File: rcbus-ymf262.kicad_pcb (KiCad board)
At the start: 2 copper layers, 100 x 50 mm, 43 parts, among them CON1 SJ1-3523N, P1 RC2014 BUS, U1 74HCT688, U2 YMF262, U3 YAC512, U4 TL074, Y1 SG-8002CA

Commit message: update url
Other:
- board text added: "https://maidavale.org/projects/rcbus-opl3/"
- board text removed: "github.com/electrified/rcbus-ymf262"

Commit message: further silkscreen tidyups
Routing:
- net +5VA: track 70.4 -> 69.4 mm
- net /AUDIO_CH2: track 24.3 -> 23.6 mm
- net /SMPBD: track 10.1 -> 9.42 mm
- net /D6: track 36.1 -> 35.5 mm
- net GND: track 47.5 -> 47.0 mm, vias 68 -> 69

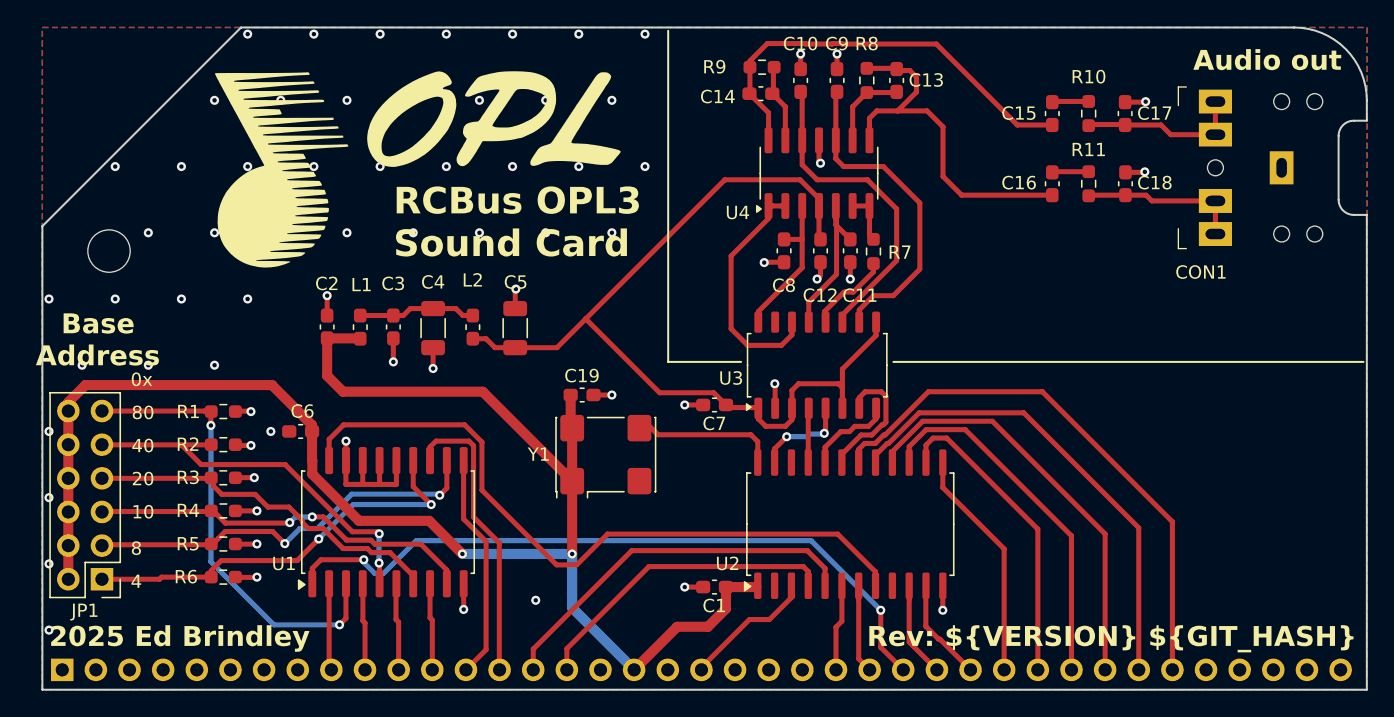
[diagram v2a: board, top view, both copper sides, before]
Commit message: remove some components, more tidyup
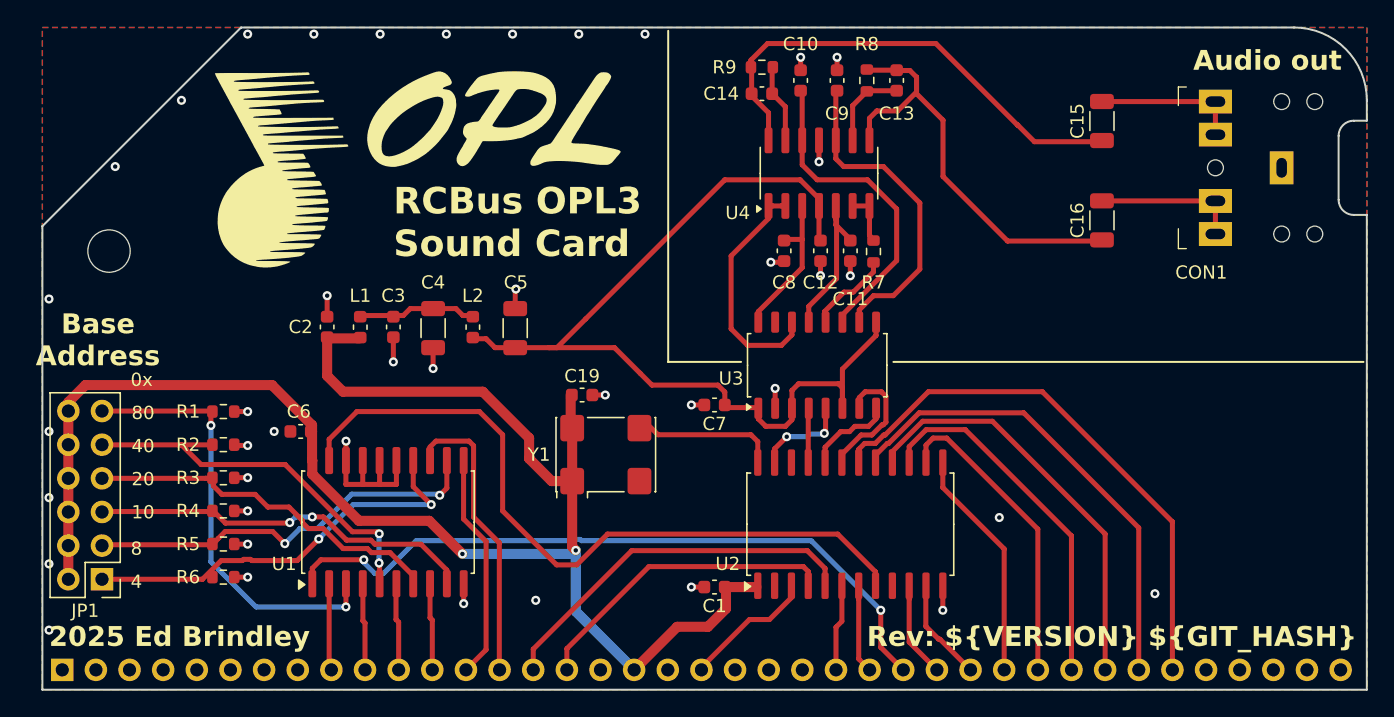
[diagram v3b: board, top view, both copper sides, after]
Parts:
- removed C17, C18: 3.9nF, Capacitor_SMD:C_0603_1608Metric_Pad1.08x0.95mm_HandSolder
- removed R10, R11: 1K, Resistor_SMD:R_0603_1608Metric_Pad0.98x0.95mm_HandSolder
- C1, C10, C11, C12, C13, C14, C19, C2, C3, C6, C7, C8, C9: footprint Capacitor_SMD:C_0603_1608Metric_Pad1.08x0.95mm_HandSolder -> Capacitor_SMD:C_0603_1608Metric
- C15, C16: footprint Capacitor_SMD:C_0603_1608Metric_Pad1.08x0.95mm_HandSolder -> Capacitor_SMD:C_1206_3216Metric
- L1, L2: footprint Inductor_SMD:L_0603_1608Metric_Pad1.05x0.95mm_HandSolder -> Inductor_SMD:L_0603_1608Metric
- R1, R2, R3, R4, R5, R6, R7, R8, R9: footprint Resistor_SMD:R_0603_1608Metric_Pad0.98x0.95mm_HandSolder -> Resistor_SMD:R_0603_1608Metric
- moved C16 4.66 mm to (140.5, 129.1)
- moved C15 3.79 mm to (140.5, 121.6)
- moved C14 0.08 mm to (114.8, 119.5)
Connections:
- CON1 pad R: Net-(C18-Pad1) -> Net-(C16-Pad2)
- CON1 pad RN: Net-(C18-Pad1) -> Net-(C16-Pad2)
- CON1 pad T: Net-(C17-Pad1) -> Net-(C15-Pad2)
- CON1 pad TN: Net-(C17-Pad1) -> Net-(C15-Pad2)
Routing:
- net Net-(C18-Pad1): track 12.2 -> 0.00 mm
- net Net-(C17-Pad1): track 12.0 -> 0.00 mm
- net GND: track 47.0 -> 36.8 mm, vias 69 -> 41
- net Net-(C16-Pad2): track 2.70 -> 11.0 mm
- net Net-(C15-Pad2): track 2.70 -> 11.0 mm
- net /R: track 27.5 -> 33.3 mm
- net /L: track 32.5 -> 36.6 mm
- net +5VA: track 69.4 -> 71.8 mm
- net /~{CS}: track 53.0 -> 55.1 mm
- net Net-(JP1-Pin_11): track 34.3 -> 32.7 mm
- net VCC: track 121.9 -> 123.3 mm
